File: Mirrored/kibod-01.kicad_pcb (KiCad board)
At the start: 2 copper layers, 155.2 x 87.6 mm, 46 parts, among them J1 02x05, J2 02x05, U1 ProMicro, U2 trrs

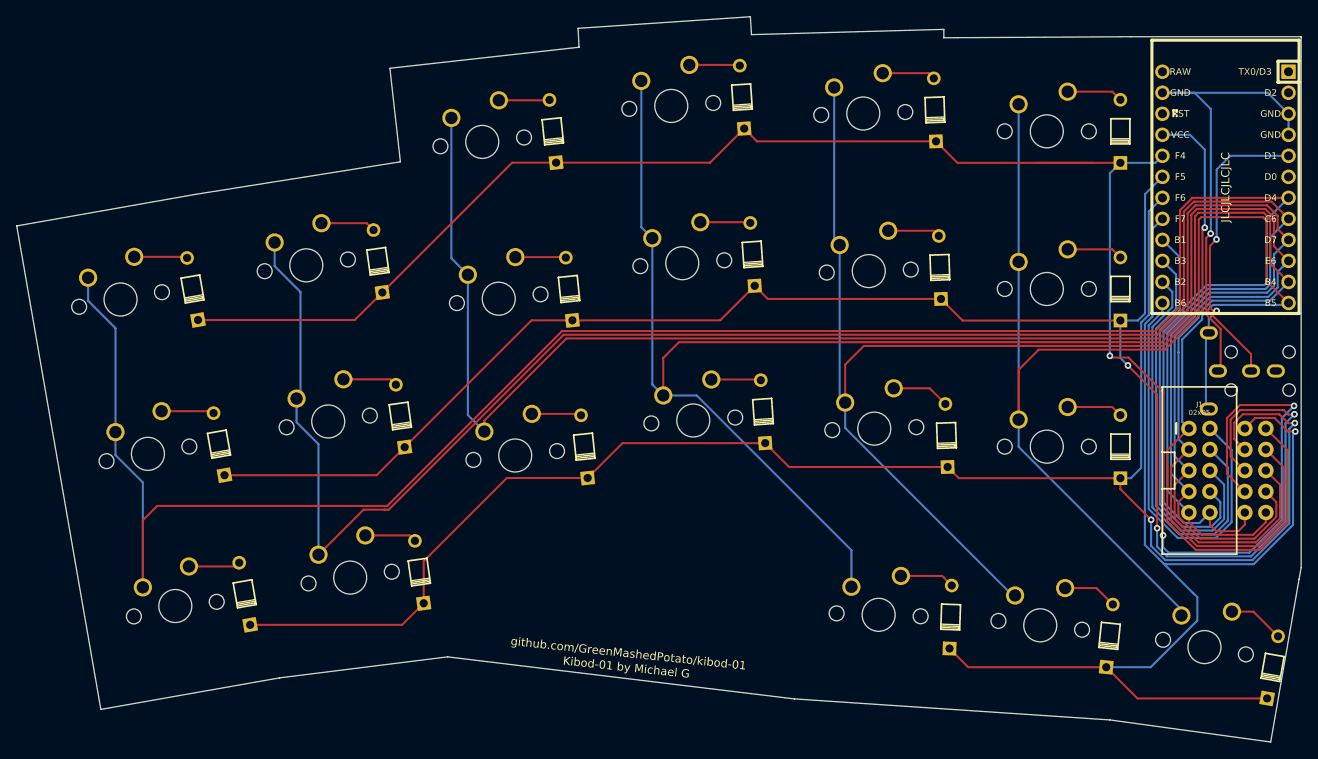
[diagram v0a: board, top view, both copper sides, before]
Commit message: fix gerber error jlcpcb
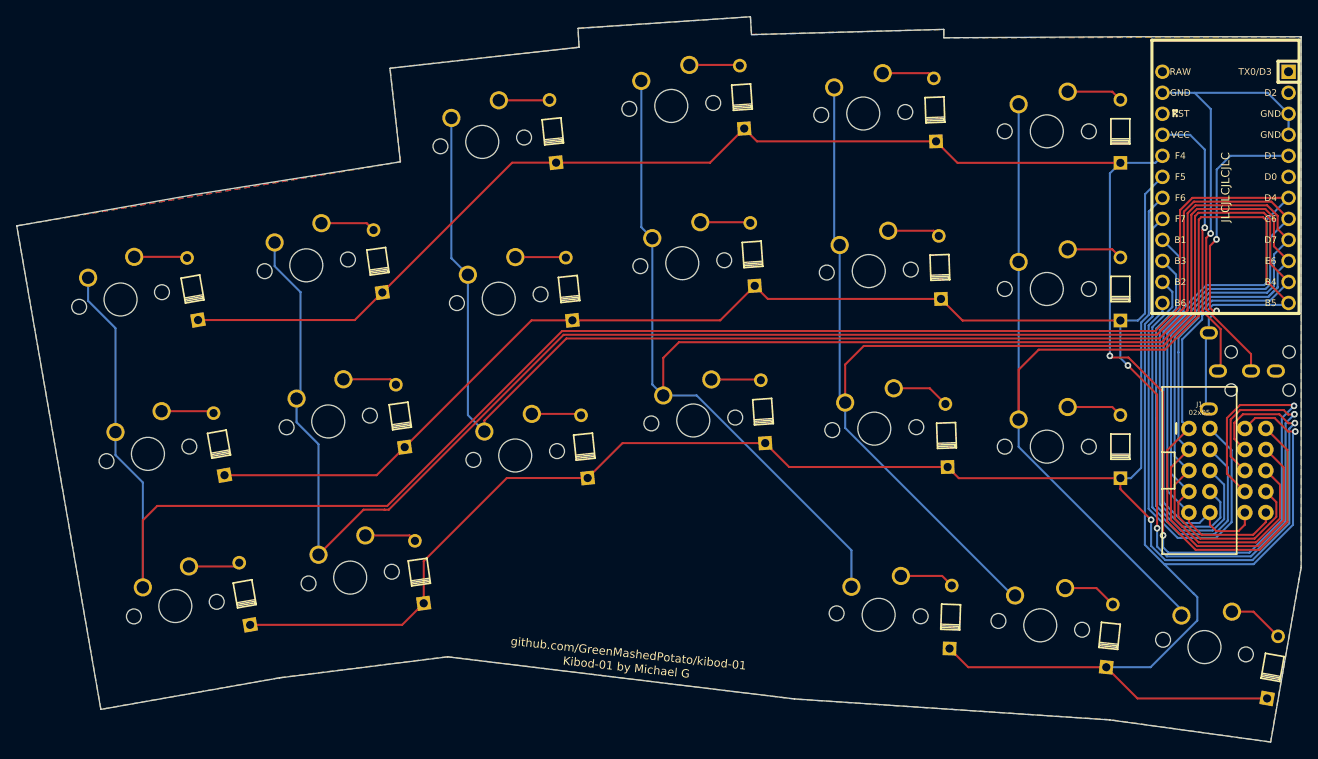
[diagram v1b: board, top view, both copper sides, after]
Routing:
- net RL0: track 235.0 -> 228.3 mm
- net GND: track 59.6 -> 55.7 mm
- added copper zone on B.Cu, net (none)
- added copper zone on F.Cu, net (none)
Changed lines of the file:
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@@
       (layerselection 0x003ffff_ffffffff)
       (disableapertmacros false)
-      (usegerberextensions false)
+      (usegerberextensions true)
       (usegerberattributes true)
       (usegerberadvancedattributes true)
@@
   (segment (start 53.232371 52.388457) (end 56.559761 49.061067) (width 0.25) (layer "F.Cu") (net 16))
   (segment (start 146.713325 56.916739) (end 144.672711 56.916739) (width 0.25) (layer "F.Cu") (net 16))
-  (segment (start 136.646311 33.396339) (end 135.630311 33.396339) (width 0.25) (layer "F.Cu") (net 16))
   (segment (start 158.61296 70.945219) (end 160.776311 73.10857) (width 0.25) (layer "F.Cu") (net 16))
   (segment (start 126.05865 33.396339) (end 123.462478 30.800167) (width 0.25) (layer "F.Cu") (net 16))
-  (segment (start 135.630311 33.396339) (end 142.386711 33.396339) (width 0.25) (layer "F.Cu") (net 16))
+  (segment (start 126.05865 33.396339) (end 145.739511 33.396339) (width 0.25) (layer "F.Cu") (net 16))
   (segment (start 166.618311 62.657139) (end 166.719911 62.758739) (width 0.25) (layer "F.Cu") (net 16))
-  (segment (start 145.739511 33.396339) (end 142.386711 33.396339) (width 0.25) (layer "F.Cu") (net 16))
   (segment (start 150.900324 78.405139) (end 150.900324 61.103738) (width 0.25) (layer "F.Cu") (net 16))
   (segment (start 101.833791 30.800167) (end 123.462478 30.800167) (width 0.25) (layer "F.Cu") (net 16))
@@
   (segment (start 100.285283 29.251659) (end 101.833791 30.800167) (width 0.25) (layer "F.Cu") (net 16))
   (segment (start 150.900324 61.103738) (end 146.713325 56.916739) (width 0.25) (layer "F.Cu") (net 16))
-  (segment (start 142.386711 33.396339) (end 136.646311 33.396339) (width 0.25) (layer "F.Cu") (net 16))
   (segment (start 160.191393 62.657139) (end 166.618311 62.657139) (width 0.25) (layer "F.Cu") (net 16))
-  (segment (start 135.630311 33.396339) (end 126.05865 33.396339) (width 0.25) (layer "F.Cu") (net 16))
   (segment (start 144.672711 56.916739) (end 144.469511 56.713539) (width 0.25) (layer "F.Cu") (net 16))
   (via (at 166.719911 62.758739) (size 0.8) (drill 0.4) (layers "F.Cu" "B.Cu") (net 16))
@@
   (segment (start 154.693911 24.926339) (end 156.663723 26.896151) (width 0.25) (layer "B.Cu") (net 19))
   (segment (start 156.663723 41.919637) (end 156.645967 41.937393) (width 0.25) (layer "B.Cu") (net 19))
-  (segment (start 150.819511 24.926339) (end 154.693911 24.926339) (width 0.25) (layer "B.Cu") (net 19))
   (segment (start 150.819511 24.926339) (end 163.519511 24.926339) (width 0.25) (layer "B.Cu") (net 19))
   (segment (start 163.519511 24.926339) (end 166.059511 27.466339) (width 0.25) (layer "B.Cu") (net 19))
@@
   (segment (start 154.557399 85.394227) (end 155.035911 85.872739) (width 0.25) (layer "B.Cu") (net 28))
   (segment (start 154.539071 85.394227) (end 154.557399 85.394227) (width 0.25) (layer "B.Cu") (net 28))
-  (segment (start 150.886547 81.741703) (end 151.029783 81.884939) (width 0.25) (layer "B.Cu") (net 28))
   (segment (start 148.699511 52.873108) (end 149.6187 51.953918) (width 0.25) (layer "B.Cu") (net 28))
-  (segment (start 150.886547 81.741703) (end 148.699511 79.554667) (width 0.25) (layer "B.Cu") (net 28))
   (segment (start 149.6187 41.36715) (end 150.819511 40.166339) (width 0.25) (layer "B.Cu") (net 28))
   (segment (start 149.6187 51.953918) (end 149.6187 41.36715) (width 0.25) (layer "B.Cu") (net 28))
@@
   (segment (start 166.59732 77.133977) (end 166.59732 66.13253) (width 0.25) (layer "B.Cu") (net 28))
   (segment (start 151.029783 81.884939) (end 161.846359 81.884939) (width 0.25) (layer "B.Cu") (net 28))
-  (segment (start 150.886547 81.741703) (end 154.539071 85.394227) (width 0.25) (layer "B.Cu") (net 28))
+  (segment (start 148.699511 79.554667) (end 154.539071 85.394227) (width 0.25) (layer "B.Cu") (net 28))
   (segment (start 148.699511 79.554667) (end 148.699511 52.873108) (width 0.25) (layer "B.Cu") (net 28))
   (segment (start 155.035911 88.695387) (end 149.395832 94.335467) (width 0.25) (layer "B.Cu") (net 28))
@@
   (segment (start 152.300391 76.352774) (end 152.300391 72.28809) (width 0.25) (layer "F.Cu") (net 34))
   (segment (start 165.030142 76.358464) (end 162.133236 79.25537) (width 0.25) (layer "F.Cu") (net 34))
-  (segment (start 164.7444 48.465732) (end 164.7444 46.56145) (width 0.25) (layer "B.Cu") (net 34))
-  (segment (start 164.7444 46.56145) (end 166.059511 45.246339) (width 0.25) (layer "B.Cu") (net 34))
   (segment (start 87.8497 41.168011) (end 89.17856 42.496871) (width 0.25) (layer "B.Cu") (net 34))
   (segment (start 154.019911 70.56857) (end 152.3051 68.853759) (width 0.25) (layer "B.Cu") (net 34))
@@
   (segment (start 152.3051 54.35326) (end 154.717442 51.940918) (width 0.25) (layer "B.Cu") (net 34))
   (segment (start 113.24148 80.202257) (end 94.53969 61.500467) (width 0.25) (layer "B.Cu") (net 34))
+  (segment (start 163.589059 49.593859) (end 164.7444 48.438518) (width 0.25) (layer "B.Cu") (net 34))
   (segment (start 89.17856 60.171606) (end 90.507421 61.500467) (width 0.25) (layer "B.Cu") (net 34))
-  (segment (start 166.059511 45.920691) (end 166.059511 45.246339) (width 0.25) (layer "B.Cu") (net 34))
   (segment (start 94.53969 61.500467) (end 90.507421 61.500467) (width 0.25) (layer "B.Cu") (net 34))
-  (segment (start 163.616273 49.593859) (end 164.7444 48.465732) (width 0.25) (layer "B.Cu") (net 34))
-  (segment (start 156.616955 49.593859) (end 161.581431 49.593859) (width 0.25) (layer "B.Cu") (net 34))
-  (segment (start 162.242141 49.593859) (end 163.616273 49.593859) (width 0.25) (layer "B.Cu") (net 34))
-  (segment (start 166.059511 45.246339) (end 165.33185 45.974) (width 0.25) (layer "B.Cu") (net 34))
+  (segment (start 166.059511 45.246339) (end 164.7444 46.56145) (width 0.25) (layer "B.Cu") (net 34))
+  (segment (start 156.616955 49.593859) (end 163.616273 49.593859) (width 0.25) (layer "B.Cu") (net 34))
   (segment (start 154.717442 51.940918) (end 154.717442 51.493372) (width 0.25) (layer "B.Cu") (net 34))
   (segment (start 113.24148 84.619498) (end 113.24148 80.202257) (width 0.25) (layer "B.Cu") (net 34))
   (segment (start 89.17856 42.496871) (end 89.17856 60.171606) (width 0.25) (layer "B.Cu") (net 34))
-  (segment (start 161.581431 49.593859) (end 162.242141 49.593859) (width 0.25) (layer "B.Cu") (net 34))
-  (segment (start 162.242141 49.593859) (end 162.386343 49.593859) (width 0.25) (layer "B.Cu") (net 34))
+  (segment (start 164.7444 48.465732) (end 163.616273 49.593859) (width 0.25) (layer "B.Cu") (net 34))
   (segment (start 154.717442 51.493372) (end 156.616955 49.593859) (width 0.25) (layer "B.Cu") (net 34))
+  (segment (start 164.7444 46.56145) (end 164.7444 48.465732) (width 0.25) (layer "B.Cu") (net 34))
   (segment (start 152.3051 68.853759) (end 152.3051 54.35326) (width 0.25) (layer "B.Cu") (net 34))
   (segment (start 158.724732 76.628475) (end 157.089808 78.263399) (width 0.25) (layer "B.Cu") (net 35))
@@
   (segment (start 139.369511 24.796339) (end 144.759511 24.796339) (width 0.25) (layer "F.Cu") (net 44))
   (segment (start 144.759511 24.796339) (end 145.739511 25.776339) (width 0.25) (layer "F.Cu") (net 44))
+  (zone (net 0) (net_name "") (layer "F.Cu") (hatch edge 0.508)
+    (connect_pads (clearance 0.508))
+    (min_thickness 0.254) (filled_areas_thickness no)
+    (fill yes (thermal_gap 0.508) (thermal_bridge_width 0.508))
+    (polygon
+      (pts
+        (xy 101.1428 17.8816)
+        (xy 124.4092 17.272)
+        (xy 124.4092 18.288)
+        (xy 167.5892 18.1864)
+        (xy 167.5892 82.296)
+        (xy 163.8808 103.3272)
+        (xy 163.8808 103.378)
+        (xy 144.526 100.6856)
+        (xy 106.6292 98.1964)
+        (xy 64.4652 93.0656)
+        (xy 44.1452 95.6056)
+        (xy 22.6568 99.4156)
+        (xy 22.5552 99.4156)
+        (xy 12.3952 40.9956)
+        (xy 58.7756 33.274)
+        (xy 57.5056 22.0472)
+        (xy 57.5056 21.9456)
+        (xy 80.3148 19.4056)
+        (xy 80.2132 17.1196)
+        (xy 101.0412 15.748)
+      )
+    )
+  )
+  (zone (net 0) (net_name "") (layer "B.Cu") (hatch edge 0.508)
+    (connect_pads (clearance 0.508))
+    (min_thickness 0.254) (filled_areas_thickness no)
+    (fill yes (thermal_gap 0.508) (thermal_bridge_width 0.508))
+    (polygon
+      (pts
+        (xy 101.1936 17.9324)
+        (xy 124.4092 17.272)
+        (xy 124.4092 18.288)
+        (xy 167.5892 18.1864)
+        (xy 167.5892 82.2452)
+        (xy 163.8808 103.378)
+        (xy 144.4752 100.6856)
+        (xy 106.426 98.1964)
+        (xy 64.4652 93.0656)
+        (xy 44.1452 95.6056)
+        (xy 22.606 99.4156)
+        (xy 22.5552 99.4156)
+        (xy 12.3952 41.0464)
+        (xy 12.3952 40.9956)
+        (xy 58.7248 33.274)
+        (xy 57.5056 22.098)
+        (xy 57.5056 21.9456)
+        (xy 80.3148 19.4564)
+        (xy 80.3148 19.4056)
+        (xy 80.2132 17.1704)
+        (xy 101.0412 15.748)
+      )
+    )
+  )
 )

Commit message: fixed non reversible holes
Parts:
- K-0-0, K-0-1, K-0-2, K-0-3, K-0-4, K-0-5, K-1-0, K-1-1, K-1-2, K-1-3, K-1-4, K-1-5, K-2-0, K-2-1, K-2-2, K-2-3, K-2-4, K-2-5, K-3-3, K-3-4, K-3-5: footprint footprints:100-minimal-no-3d -> footprints:100-dual
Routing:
- net CL5: track 198.6 -> 200.7 mm
- net CL3: track 238.7 -> 236.8 mm
- net CL4: track 213.2 -> 211.3 mm
- net RL3: track 142.5 -> 144.2 mm
- net RL2: track 209.0 -> 208.3 mm
